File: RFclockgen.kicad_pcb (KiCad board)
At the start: 2 copper layers, 1 part, among them U1 ADF4351BCPZ-RL7

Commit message: Added more components!
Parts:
- added L1: LQW15AN18NJ00D, LQW15AN18NJ00D:INDC1006X60N, F.Cu at (123.8, 73.9)
- added U2: ESP32-S3-WROOM-1, RF_Module:ESP32-S3-WROOM-1, F.Cu at (155.2, 61.2)
- added U3: AP2112K-3.3, Package_TO_SOT_SMD:SOT-23-5, F.Cu at (124.9, 70.5)
- added XTAL1: TSX-3225 24.0000MF20G-AC3, TSX_3225_24_0000MF20G_AC3:TSX-3225 24.0000MF20G-AC3_EPS, F.Cu at (134.3, 77.8)

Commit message: Added items to PCB
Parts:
- added C1: 1u, Capacitor_SMD:C_0805_2012Metric_Pad1.18x1.45mm_HandSolder, F.Cu at (98.8, 82.9)
- added C10: 10p, Capacitor_SMD:C_0805_2012Metric_Pad1.18x1.45mm_HandSolder, F.Cu at (82.4, 88.6)
- added C11: 0.1u, Capacitor_SMD:C_0805_2012Metric_Pad1.18x1.45mm_HandSolder, F.Cu at (82.4, 91.6)
- added C12: 10p, Capacitor_SMD:C_0805_2012Metric_Pad1.18x1.45mm_HandSolder, F.Cu at (82.4, 94.6)
- added C13: 0.1u, Capacitor_SMD:C_0805_2012Metric_Pad1.18x1.45mm_HandSolder, F.Cu at (87.2, 79.6)
- added C14: 0.1uF, Capacitor_SMD:C_0805_2012Metric_Pad1.18x1.45mm_HandSolder, F.Cu at (87.2, 82.6)
- added C15: 0.1uF, Capacitor_SMD:C_0805_2012Metric_Pad1.18x1.45mm_HandSolder, F.Cu at (87.2, 85.6)
- added C16: 10pF, Capacitor_SMD:C_0805_2012Metric_Pad1.18x1.45mm_HandSolder, F.Cu at (87.2, 88.6)
- added C17: 10pF, Capacitor_SMD:C_0805_2012Metric_Pad1.18x1.45mm_HandSolder, F.Cu at (87.2, 91.6)
- added C18: 15nF, Capacitor_SMD:C_0805_2012Metric_Pad1.18x1.45mm_HandSolder, F.Cu at (87.2, 94.6)
- added C19: 22nF, Capacitor_SMD:C_0805_2012Metric_Pad1.18x1.45mm_HandSolder, F.Cu at (92.0, 79.6)
- added C2: 1u, Capacitor_SMD:C_0805_2012Metric_Pad1.18x1.45mm_HandSolder, F.Cu at (98.8, 85.9)
- added C20: 330pF, Capacitor_SMD:C_0805_2012Metric_Pad1.18x1.45mm_HandSolder, F.Cu at (92.0, 82.6)
- added C21: 1n, Capacitor_SMD:C_0805_2012Metric_Pad1.18x1.45mm_HandSolder, F.Cu at (92.0, 85.6)
- added C22: 1n, Capacitor_SMD:C_0805_2012Metric_Pad1.18x1.45mm_HandSolder, F.Cu at (92.0, 88.6)
- added C23: 10uF, Capacitor_SMD:C_0805_2012Metric_Pad1.18x1.45mm_HandSolder, F.Cu at (98.0, 113.0)
- added C24: 10uF, Capacitor_SMD:C_0805_2012Metric_Pad1.18x1.45mm_HandSolder, F.Cu at (82.5, 108.8)
- added C25: 1uF, Capacitor_SMD:C_0805_2012Metric_Pad1.18x1.45mm_HandSolder, F.Cu at (82.5, 111.8)
- added C26: NC, Capacitor_SMD:C_0805_2012Metric_Pad1.18x1.45mm_HandSolder, F.Cu at (66.4, 118.7)
- added C27: 0.1uF, Capacitor_SMD:C_0805_2012Metric_Pad1.18x1.45mm_HandSolder, F.Cu at (124.5, 140.5)
- added C28: 0.1uF, Capacitor_SMD:C_0805_2012Metric_Pad1.18x1.45mm_HandSolder, F.Cu at (124.5, 143.5)
- added C3: 0.1u, Capacitor_SMD:C_0805_2012Metric_Pad1.18x1.45mm_HandSolder, F.Cu at (98.8, 88.9)
- added C4: 1u, Capacitor_SMD:C_0805_2012Metric_Pad1.18x1.45mm_HandSolder, F.Cu at (98.8, 91.9)
- added C5: 0.1u, Capacitor_SMD:C_0805_2012Metric_Pad1.18x1.45mm_HandSolder, F.Cu at (98.8, 94.9)
- added C6: 22u, Capacitor_SMD:C_0805_2012Metric_Pad1.18x1.45mm_HandSolder, F.Cu at (98.8, 97.9)
- added C7: 1u, Capacitor_SMD:C_0805_2012Metric_Pad1.18x1.45mm_HandSolder, F.Cu at (82.4, 79.6)
- added C8: 10p, Capacitor_SMD:C_0805_2012Metric_Pad1.18x1.45mm_HandSolder, F.Cu at (82.4, 82.6)
- added C9: 0.1u, Capacitor_SMD:C_0805_2012Metric_Pad1.18x1.45mm_HandSolder, F.Cu at (82.4, 85.6)
- added D1: 1N5819, Diode_THT:D_DO-41_SOD81_P10.16mm_Horizontal, F.Cu at (88.8, 109.4)
- added D2: ESD9B5.0ST5G, Diode_SMD:D_SOD-923, F.Cu at (94.3, 112.5)
- added D3: ESD9B5.0ST5G, Diode_SMD:D_SOD-923, F.Cu at (94.3, 114.4)
- added D4: ESD9B5.0ST5G, Diode_SMD:D_SOD-923, F.Cu at (94.3, 116.4)
- added D5: WS2812B, LED_SMD:LED_WS2812B_PLCC4_5.0x5.0mm_P3.2mm, F.Cu at (68.1, 110.6)
- added D6: 1N4148W, Diode_SMD:D_SOD-123, F.Cu at (67.0, 115.5)
- added J4: Conn_Coaxial, Connector_Coaxial:SMA_Samtec_SMA-J-P-H-ST-EM1_EdgeMount, F.Cu at (61.4, 82.6)
- added J5: Conn_Coaxial, Connector_Coaxial:SMA_Samtec_SMA-J-P-H-ST-EM1_EdgeMount, F.Cu at (61.4, 91.7)
- added J6: Conn_Coaxial, Connector_Coaxial:SMA_Samtec_SMA-J-P-H-ST-EM1_EdgeMount, F.Cu at (61.4, 100.7)
- added R1: 10k, Resistor_SMD:R_1206_3216Metric_Pad1.30x1.75mm_HandSolder, F.Cu at (99.4, 79.7)
- added R10: 5.1k, Resistor_SMD:R_1206_3216Metric_Pad1.30x1.75mm_HandSolder, F.Cu at (89.9, 116.5)
- added R11: 10k, Resistor_SMD:R_1206_3216Metric_Pad1.30x1.75mm_HandSolder, F.Cu at (77.1, 108.9)
- added R12: 47.5k, Resistor_SMD:R_1206_3216Metric_Pad1.30x1.75mm_HandSolder, F.Cu at (77.1, 112.2)
- added R13: 10k, Resistor_SMD:R_1206_3216Metric_Pad1.30x1.75mm_HandSolder, F.Cu at (77.1, 115.5)
- added R14: 10k, Resistor_SMD:R_1206_3216Metric_Pad1.30x1.75mm_HandSolder, F.Cu at (77.1, 118.8)
- added R15: 0, Resistor_SMD:R_1206_3216Metric_Pad1.30x1.75mm_HandSolder, F.Cu at (77.1, 122.1)
- added R16: 0, Resistor_SMD:R_1206_3216Metric_Pad1.30x1.75mm_HandSolder, F.Cu at (77.1, 125.5)
- added R17: 0, Resistor_SMD:R_1206_3216Metric_Pad1.30x1.75mm_HandSolder, F.Cu at (61.1, 108.9)
- added R18: 0, Resistor_SMD:R_1206_3216Metric_Pad1.30x1.75mm_HandSolder, F.Cu at (61.1, 112.2)
- added R19: 10k, Resistor_SMD:R_1206_3216Metric_Pad1.30x1.75mm_HandSolder, F.Cu at (61.1, 115.5)
- added R2: 1k, Resistor_SMD:R_1206_3216Metric_Pad1.30x1.75mm_HandSolder, F.Cu at (77.0, 79.7)
- added R20: 0, Resistor_SMD:R_1206_3216Metric_Pad1.30x1.75mm_HandSolder, F.Cu at (61.1, 118.8)
- added R21: 4.7k, Resistor_SMD:R_1206_3216Metric_Pad1.30x1.75mm_HandSolder, F.Cu at (61.1, 122.1)
- added R22: 10k, Resistor_SMD:R_1206_3216Metric_Pad1.30x1.75mm_HandSolder, F.Cu at (61.1, 125.5)
- added R3: 51, Resistor_SMD:R_1206_3216Metric_Pad1.30x1.75mm_HandSolder, F.Cu at (77.0, 83.0)
- added R4: 390, Resistor_SMD:R_1206_3216Metric_Pad1.30x1.75mm_HandSolder, F.Cu at (77.0, 86.3)
- added R5: 750, Resistor_SMD:R_1206_3216Metric_Pad1.30x1.75mm_HandSolder, F.Cu at (77.0, 89.7)
- added R6: 51, Resistor_SMD:R_1206_3216Metric_Pad1.30x1.75mm_HandSolder, F.Cu at (77.0, 93.0)
- added R7: 51, Resistor_SMD:R_1206_3216Metric_Pad1.30x1.75mm_HandSolder, F.Cu at (77.0, 96.3)
- added R8: 4.7k, Resistor_SMD:R_1206_3216Metric_Pad1.30x1.75mm_HandSolder, F.Cu at (77.0, 99.6)
- added R9: 5.1k, Resistor_SMD:R_1206_3216Metric_Pad1.30x1.75mm_HandSolder, F.Cu at (89.9, 113.2)
- added U1: ADF4351, Package_CSP:LFCSP-32-1EP_5x5mm_P0.5mm_EP3.25x3.25mm, F.Cu at (83.5, 99.7)
- added U2: AP2112K-3.3, Package_TO_SOT_SMD:SOT-23-5, F.Cu at (89.6, 98.5)
- added Y2: TG2520SMN-xx.xxxxxxMhz-xxxxNM, Oscillator:Oscillator_SMD_SeikoEpson_TG2520SMN-xxx-xxxxxx-4Pin_2.5x2.0mm, F.Cu at (89.0, 103.0)
- moved U2 24.6 mm to (178.1, 52.1)
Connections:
- U3 pad 1: unconnected-(U3-VIN-Pad1) -> +5V
- U3 pad 2: unconnected-(U3-GND-Pad2) -> GND
- U3 pad 3: unconnected-(U3-EN-Pad3) -> +5V
- U3 pad 5: unconnected-(U3-VOUT-Pad5) -> Net-(U3-VOUT)

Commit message: Actually started on PCB layout
Started the USB C connector
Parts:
- removed the U1 at (150.6, 100.8)
- removed the U2 at (178.1, 52.1)
- added FB1: 600, Inductor_SMD:L_1206_3216Metric_Pad1.22x1.90mm_HandSolder, F.Cu at (58.9, 142.3)
- added FB2: 600, Inductor_SMD:L_1206_3216Metric_Pad1.22x1.90mm_HandSolder, F.Cu at (58.9, 145.5)
- added J1: Conn_01x04_Pin, Connector_PinHeader_1.00mm:PinHeader_1x04_P1.00mm_Vertical, F.Cu at (68.5, 170.0)
- added J2: USB_C_Receptacle_USB2.0_16P, Connector_USB:USB_C_Receptacle_GCT_USB4105-xx-A_16P_TopMnt_Horizontal, F.Cu at (251.6, 132.1)
- added J3: Conn_01x02_Pin, Connector_PinHeader_1.00mm:PinHeader_1x02_P1.00mm_Vertical, F.Cu at (71.8, 170.0)
- added L1: 3.9n, Inductor_SMD:L_1206_3216Metric_Pad1.22x1.90mm_HandSolder, F.Cu at (65.3, 142.1)
- added L2: 3.9n, Inductor_SMD:L_1206_3216Metric_Pad1.22x1.90mm_HandSolder, F.Cu at (65.3, 145.5)
- added S1: TL1105AF160Q, TL1105AF160Q:SW_TL1105AF160Q, F.Cu at (157.2, 138.2)
- added S2: TL1105AF160Q, TL1105AF160Q:SW_TL1105AF160Q, F.Cu at (157.2, 145.8)
- added U4: ESP32-C6-WROOM-1-N8, ESP32-C6-WROOM-1:MOD28_ESP32-C6-WROOM-1_EXP, F.Cu at (215.8, 59.5)
- added U5: BC847BDW1T1G, BC847BDW1T1G:SOT-363-6_2P2X1P35_ONS, F.Cu at (237.0, 116.9)
- added U6: CP2102N-A02-GQFN28, CP2102N_A02_GQFN28:QFN28_5X5, F.Cu at (251.6, 116.7)
- D2, D3: footprint Diode_SMD:D_SOD-923 -> Diode_SMD:D_SOD-323F
- D4: value ESD9B5.0ST5G -> ESD9C5.0ST5G; footprint Diode_SMD:D_SOD-923 -> Diode_SMD:D_SOD-323F
- moved R14 185.4 mm to (262.5, 115.0), turned to 180 degrees
- moved R13 185.4 mm to (262.5, 118.0)
- moved R12 183.6 mm to (260.5, 122.0), turned to -90 degrees
- moved R11 182.7 mm to (259.0, 126.0)
- moved C25 181.3 mm to (263.5, 122.0), turned to -90 degrees
- moved C24 175.5 mm to (257.5, 122.0), turned to 90 degrees
- moved R9 165.4 mm to (255.0, 122.5), turned to -90 degrees
- moved D4 158.4 mm to (252.4, 124.8), turned to -90 degrees
- moved R10 157.7 mm to (247.4, 124.6), turned to -90 degrees
- moved D2 156.6 mm to (250.4, 124.8), turned to -90 degrees
- moved D1 155.1 mm to (242.5, 129.7), turned to 180 degrees
- moved R15 146.3 mm to (219.0, 86.3)
- moved R16 146.3 mm to (219.0, 89.6)
- moved J4 145.1 mm to (198.1, 131.3), turned to -90 degrees
- moved C23 145.0 mm to (242.4, 125.7), turned to 90 degrees
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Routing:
- net VBUSA: track 0.00 -> 37.7 mm
- net Net-(U6-VBUS): track 0.00 -> 17.0 mm
- net USB_D+: track 0.00 -> 12.4 mm
- net USB_D-: track 0.00 -> 12.2 mm, vias 0 -> 2
- net Net-(U6-SUSPENDB): track 0.00 -> 7.72 mm
- net Net-(U6-RSTB): track 0.00 -> 7.15 mm
- net +3.3V: track 0.00 -> 6.21 mm
- net Net-(J2-CC2): track 0.00 -> 5.05 mm
- net Net-(J2-CC1): track 0.00 -> 4.22 mm
- net +5V: track 0.00 -> 3.00 mm
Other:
- board outline added: 100 x 100 mm

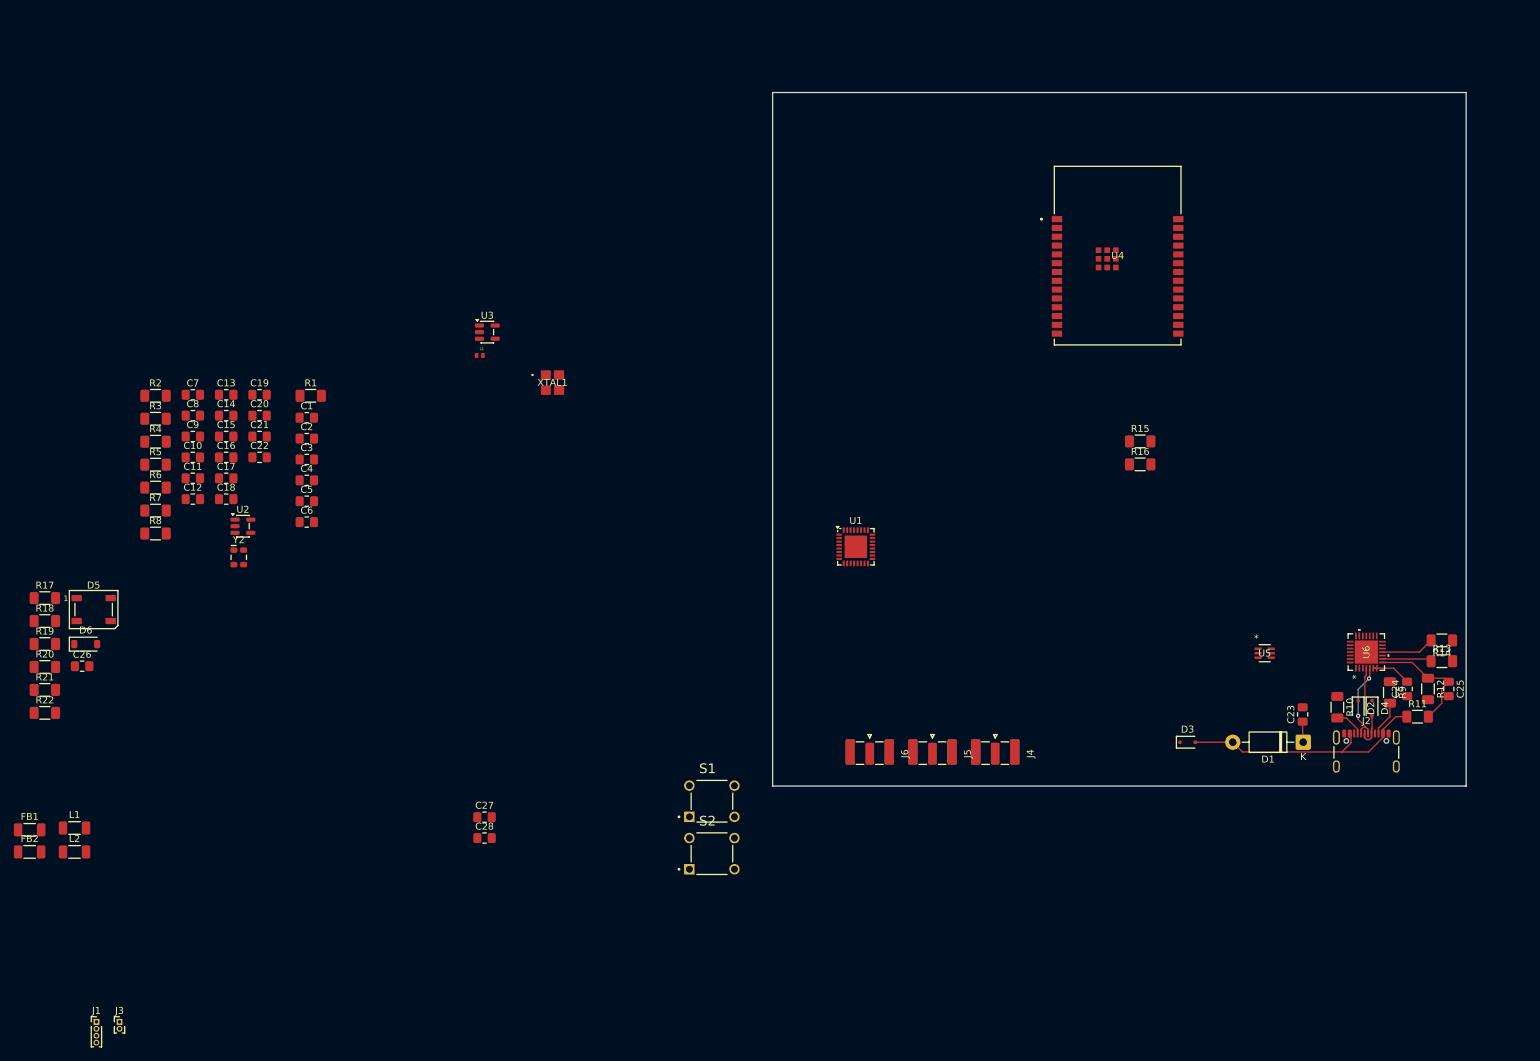
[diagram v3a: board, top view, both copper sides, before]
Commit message: Refactored most of the PCB Layout
Pretty much restarted the PCB layout to make it look a little bit nicer and easier to read.
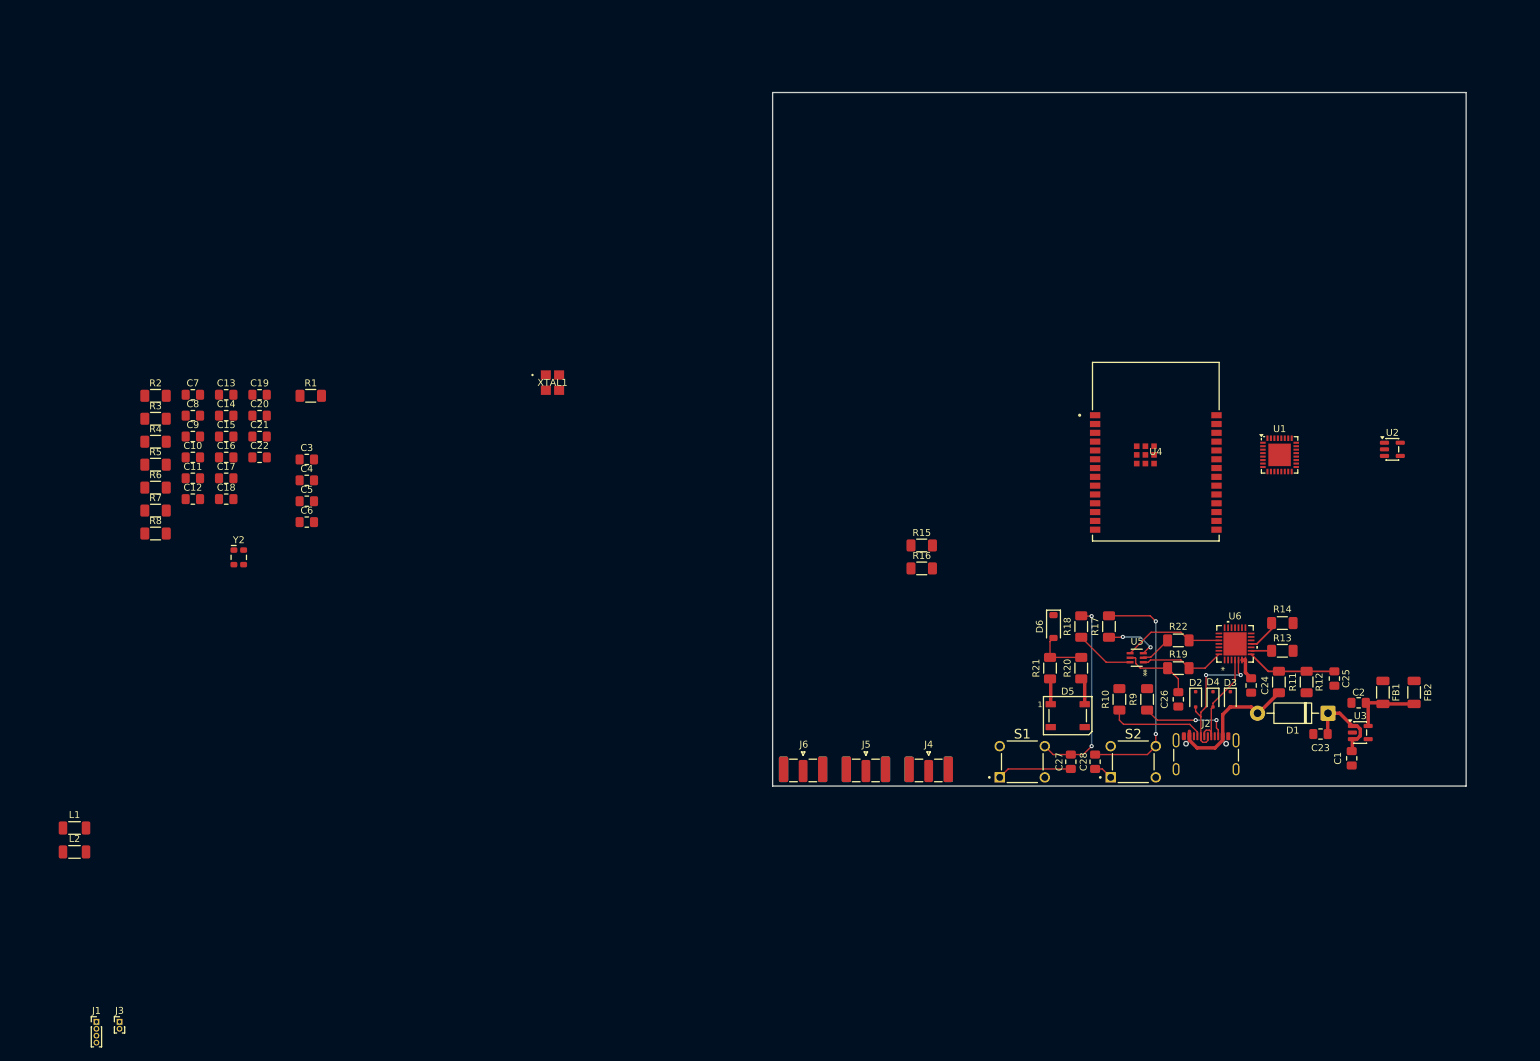
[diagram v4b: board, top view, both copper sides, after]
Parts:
- removed the L1 at (123.8, 73.9)
- moved FB2 201.0 mm to (258.5, 122.5), turned to 90 degrees
- moved FB1 196.1 mm to (254.0, 122.5), turned to -90 degrees
- moved U2 166.1 mm to (255.4, 87.5)
- moved R22 163.8 mm to (224.5, 115.0)
- moved R19 163.5 mm to (224.5, 119.0), turned to 180 degrees
- moved C1 158.5 mm to (249.5, 132.0), turned to -90 degrees
- moved C26 158.1 mm to (224.5, 123.5), turned to -90 degrees
- moved C2 156.4 mm to (250.5, 124.0), turned to 180 degrees
- moved R17 153.5 mm to (214.5, 113.0), turned to -90 degrees
- moved R18 149.4 mm to (210.5, 113.0), turned to 90 degrees
- moved R20 149.4 mm to (210.5, 119.0), turned to -90 degrees
- moved R21 145.0 mm to (206.0, 119.0), turned to -90 degrees
- moved D5 141.3 mm to (208.6, 125.8)
- moved D6 139.6 mm to (206.5, 113.0), turned to -90 degrees
- moved U3 138.5 mm to (250.7, 128.3)
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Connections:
- C3 pad 1: 3.3V -> +3.3V
- C4 pad 1: EN -> CHIP_PU
- C5 pad 2: EN -> CHIP_PU
- C6 pad 1: 3.3V -> +3.3V
- FB2 pad 2: 3.3V -> +3.3V
- R1 pad 1: EN -> CHIP_PU
- R1 pad 2: 3.3V -> +3.3V
- R13 pad 2: 3.3V -> +3.3V
- R2 pad 1: 3.3V -> +3.3V
- U1 pad 10: 3.3V -> +3.3V
- U4 pad 10: unconnected-(U4-IO8-Pad10) -> GPIO8
- U4 pad 15: Net-(J3-Pin_1) -> GPIO9
- U4 pad 2: 3.3V -> +3.3V
- U4 pad 3: EN -> CHIP_PU
- U4 pad 9: unconnected-(U4-IO1-Pad9) -> Net-(J3-Pin_1)
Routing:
- net CHIP_PU: track 0.00 -> 34.3 mm, vias 0 -> 2
- net GPIO9: track 0.00 -> 28.0 mm, vias 0 -> 2
- net VBUSA: track 37.7 -> 20.9 mm
- net RTS: track 0.00 -> 14.5 mm
- net GND: track 0.00 -> 13.5 mm
- net +5V: track 3.00 -> 16.4 mm
- net DTR: track 0.00 -> 12.3 mm
- net Net-(U5-BASE1): track 0.00 -> 10.6 mm
- net Net-(U3-VOUT): track 0.00 -> 10.5 mm
- net Net-(J2-CC1): track 4.22 -> 14.0 mm
- net Net-(U5-COLLECTOR2): track 0.00 -> 8.54 mm
- net USB_D-: track 12.2 -> 20.6 mm
- net Net-(U5-COLLECTOR1): track 0.00 -> 8.04 mm, vias 0 -> 2
- net Net-(J2-CC2): track 5.05 -> 13.0 mm, vias 0 -> 2
- net Net-(D6-A): track 0.00 -> 7.51 mm
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
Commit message: Moved some components around
No reason, just wanted to push to avoid merge conflicts
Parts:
- moved U1 15.6 mm to (240.6, 103.8)
- moved U4 8.48 mm to (221.8, 96.3)
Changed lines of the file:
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@@
 	(footprint "Package_CSP:LFCSP-32-1EP_5x5mm_P0.5mm_EP3.25x3.25mm"
 		(layer "F.Cu")
-		(at 239.1 88.25)
+		(at 240.6 103.75)
 		(descr "32-Lead Frame Chip Scale Package LFCSP (5mm x 5mm); (see http://www.analog.com/media/en/package-pcb-resources/package/pkg_pdf/lfcspcp/cp-32/CP_32_27.pdf")
 		(tags "LFCSP 0.5")
@@
 	(footprint "ESP32-C6-WROOM-1:MOD28_ESP32-C6-WROOM-1_EXP"
 		(layer "F.Cu")
-		(at 221.255 87.79)
+		(at 221.75 96.26)
 		(tags "ESP32-C6-WROOM-1-N8 ")
 		(property "Reference" "U4"
-			(at 0 0 0)
+			(at 0 -13.79 0)
 			(unlocked yes)
 			(layer "F.SilkS")
@@
 		)
 		(fp_text user "${REFERENCE}"
-			(at 0 0 0)
+			(at 0 -13.79 0)
 			(unlocked yes)
 			(layer "F.Fab")

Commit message: Same thing as last commit
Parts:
- moved J1 221.9 mm to (273.5, 85.0)
- moved J3 216.0 mm to (273.5, 92.5)
- moved R1 97.1 mm to (196.0, 89.5), turned to 90 degrees
- moved C5 92.9 mm to (191.5, 88.0)
- moved C4 92.7 mm to (191.5, 91.5), turned to 180 degrees
- moved R16 42.1 mm to (227.0, 90.0), turned to 180 degrees
- moved R15 40.2 mm to (227.0, 94.0), turned to 180 degrees
- moved U1 20.9 mm to (260.6, 97.8)
- moved U4 11.1 mm to (211.2, 92.6)
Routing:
- net CHIP_PU: track 34.3 -> 75.6 mm
- net Net-(U6-RXD): track 0.00 -> 30.1 mm, vias 0 -> 2
- net Net-(U6-TXD): track 0.00 -> 27.4 mm, vias 0 -> 2
- net +3.3V: track 3.48 -> 10.3 mm
- net UART_RXD: track 0.00 -> 6.10 mm
- net UART_TXD: track 0.00 -> 5.93 mm

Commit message: moved more stuff around on PCB layout
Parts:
- moved C28 55.7 mm to (188.0, 82.5), turned to 0 degrees
- moved S2 53.7 mm to (188.0, 88.0), turned to -90 degrees
- moved C27 36.2 mm to (225.0, 100.0), turned to 180 degrees
- moved S1 34.3 mm to (225.0, 107.0), turned to 90 degrees
- moved D5 11.6 mm to (200.0, 118.0)
- moved R20 11.6 mm to (201.9, 111.2)
- moved R21 11.6 mm to (197.4, 111.2)
- moved D6 11.4 mm to (197.5, 106.0)
- moved C5 6.32 mm to (197.5, 90.0), turned to -90 degrees
- moved R1 4.00 mm to (196.0, 85.5), turned to 0 degrees
- moved C4 2.92 mm to (194.0, 90.0), turned to 90 degrees
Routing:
- net CHIP_PU: track 75.6 -> 9.63 mm, vias 2 -> 0
- net GPIO9: track 28.0 -> 0.00 mm, vias 2 -> 0
- net GND: track 13.5 -> 2.75 mm
- net Net-(U5-COLLECTOR2): track 8.54 -> 0.00 mm
- net +3.3V: track 10.3 -> 3.48 mm
- net Net-(U5-COLLECTOR1): track 8.04 -> 1.30 mm, vias 2 -> 1
- net Net-(D6-A): track 7.51 -> 6.47 mm

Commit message: Finished PCB Layout
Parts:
- removed XTAL1: TSX-3225 24.0000MF20G-AC3, TSX_3225_24_0000MF20G_AC3:TSX-3225 24.0000MF20G-AC3_EPS
- C18: value 15nF -> 2.7nF
- C19: value 22nF -> 47nF
- C20: value 330pF -> 1.2nF
- R4: value 390 -> 360
- moved L1 170.4 mm to (226.7, 87.4), turned to -90 degrees
- moved R2 165.6 mm to (242.0, 93.6), turned to 180 degrees
- moved R3 156.5 mm to (231.6, 58.3)
- moved C10 156.0 mm to (236.4, 64.0), turned to 90 degrees
- moved C11 155.8 mm to (236.4, 68.2), turned to 90 degrees
- moved L2 154.5 mm to (211.6, 95.6)
- moved R8 154.4 mm to (227.7, 66.1), turned to -90 degrees
- moved R6 153.8 mm to (230.4, 82.2), turned to 90 degrees
- moved C12 153.0 mm to (232.4, 64.3), turned to 180 degrees
- moved C8 150.8 mm to (232.5, 67.8), turned to 180 degrees
- moved C9 150.7 mm to (232.5, 71.3), turned to 180 degrees
- moved Y2 148.6 mm to (237.3, 93.7), turned to 180 degrees
- moved C13 146.4 mm to (232.4, 60.7), turned to 180 degrees
- moved C15 142.3 mm to (226.7, 57.2)
- moved C14 141.2 mm to (226.7, 60.7), turned to 180 degrees
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- renumbered S1 to BOOT, S2 to RST
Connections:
- U1 pad 25: LD -> unconnected-(U1-LD-Pad25)
- U1 pad 28: 3.3V -> +3.3V
- U1 pad 32: 3.3V -> +3.3V
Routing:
- net +5V: track 16.4 -> 91.8 mm, vias 0 -> 3
- net Net-(U5-COLLECTOR1): track 1.30 -> 57.9 mm, vias 1 -> 2
- net VVCO: track 0.00 -> 56.5 mm, vias 0 -> 3
- net Net-(J6-Ext): track 0.00 -> 53.4 mm, vias 0 -> 3
- net RF_OUT_A+: track 0.00 -> 36.9 mm
- net RF_OUT_A-: track 0.00 -> 33.6 mm
- net VP: track 0.00 -> 33.4 mm, vias 0 -> 2
- net CHIP_PU: track 9.63 -> 40.9 mm
- net +3.3V: track 3.48 -> 31.7 mm, vias 0 -> 9
- net VTUNE: track 0.00 -> 27.9 mm, vias 0 -> 4
- net GND: track 2.75 -> 28.9 mm, vias 0 -> 227
- net DATA: track 0.00 -> 21.3 mm
- net Net-(U5-COLLECTOR2): track 0.00 -> 20.5 mm
- net VCOM: track 0.00 -> 18.8 mm, vias 0 -> 2
- net CLK: track 0.00 -> 17.5 mm, vias 0 -> 2
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- added copper zone on In2.Cu, net +3.3V
- added copper zone on B.Cu, net GND
- added copper zone on F.Cu, net GND
- added copper zone on In1.Cu, net GND
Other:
- board size 100 x 100 mm -> 87.1 x 67.4 mm
- copper layers 2 -> 4
- board text added: "O. Agenmonmen J. Binstock Rev: 1 Oct. 2026 RF Clock Generator"
